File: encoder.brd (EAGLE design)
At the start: 25.1 x 31.7 mm, 7 parts, among them SW1 ROTARTY_ENCODER

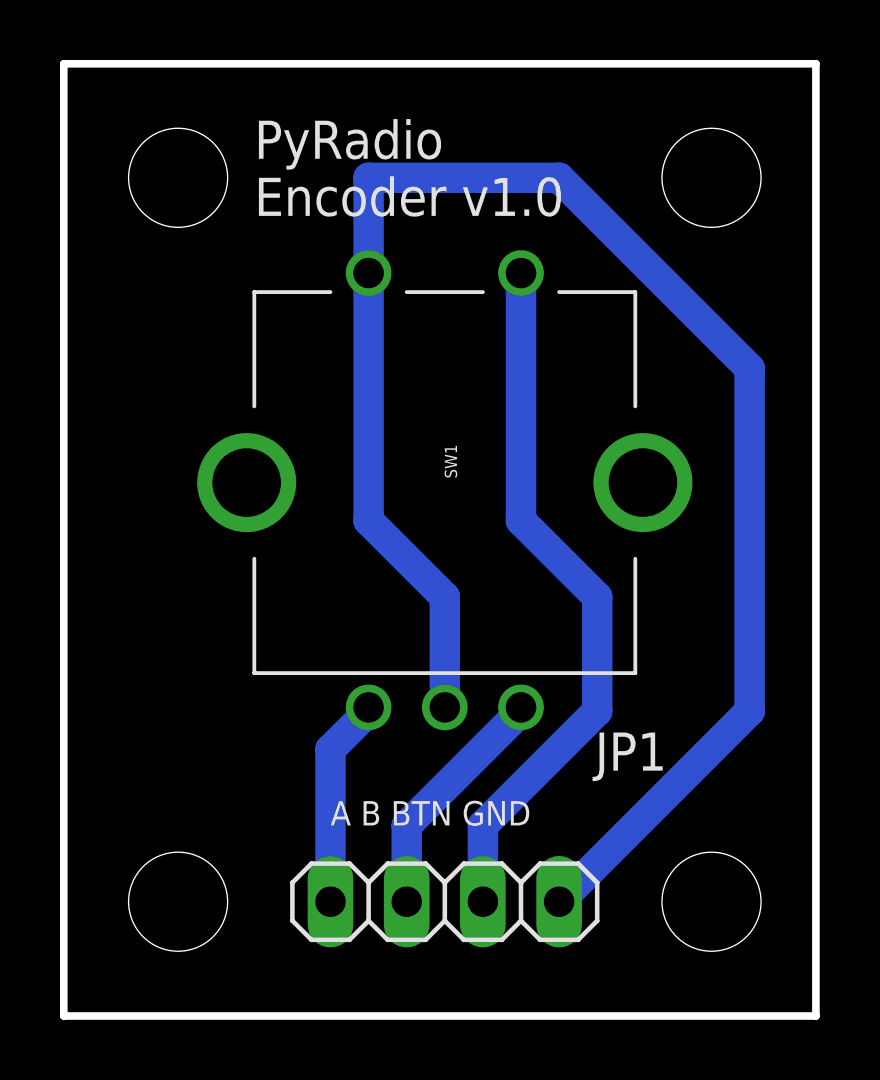
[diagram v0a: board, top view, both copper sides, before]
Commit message: pulled down all the eagle files on github.  histogram.py generates a histogram of the frequency of their usage.  You can make all the boards on github with ~1460 unique parts
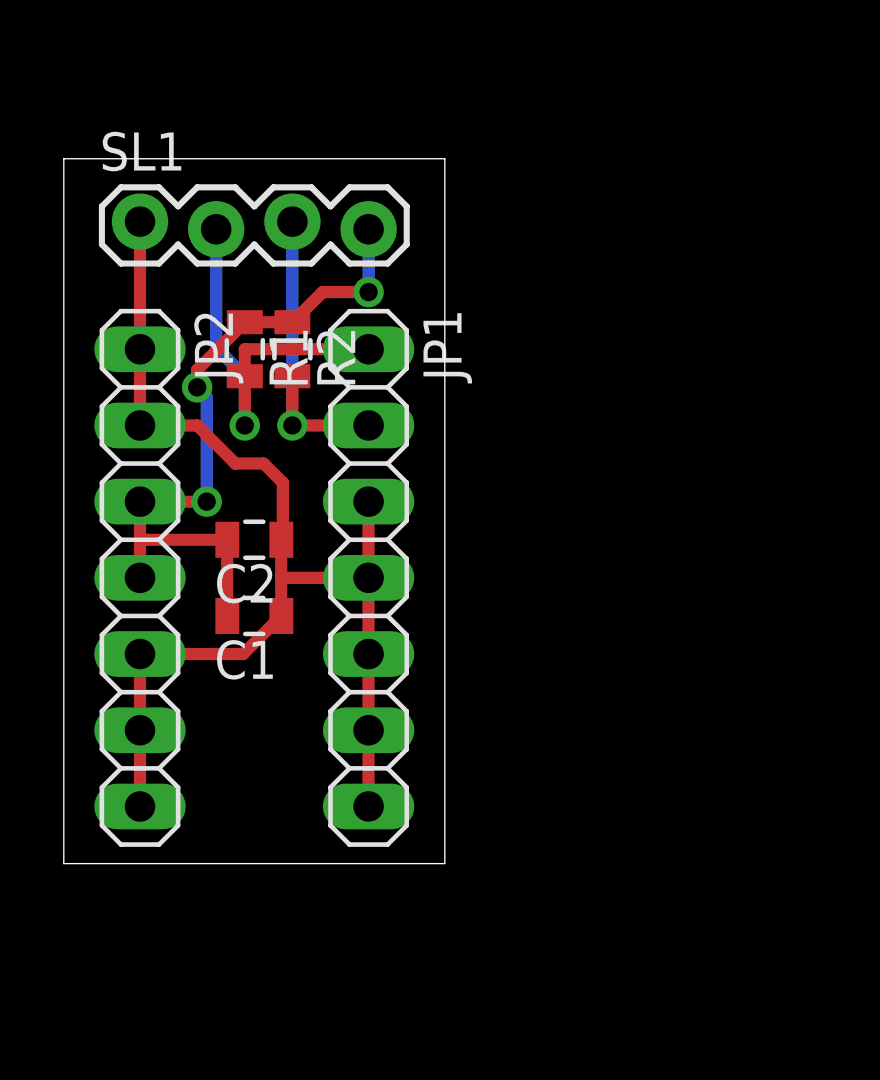
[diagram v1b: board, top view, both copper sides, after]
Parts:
- removed FRAME1: FRAME-LETTER, SparkFun-Aesthetics:CREATIVE_COMMONS
- removed STANDOFF1, STANDOFF2, STANDOFF3, STANDOFF4: STAND-OFF, SparkFun-Electromechanical:STAND-OFF
- removed SW1: ROTARTY_ENCODER, SparkFun-Electromechanical:ROTARY_ENC_PLAIN
- added C1: 47uF, ASL:0805
- added C2: .1uF, ASL:0805
- added JP2: (no value), baro:1X07
- added R1, R2: 4.7k, ASL:0805
- added SL1: (no value), ASL:1X04_LOCK
- JP1: device pinhead:1X04 -> baro:1X07
- moved JP1 11.1 mm to (10.2, 14.6), turned to 270 degrees
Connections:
- removed net A: JP1.1, SW1.A
- removed net B: JP1.2, SW1.B
- removed net BTN: JP1.3, SW1.SW+
- new net N$1: JP1.1, R1.2, SL1.2
- new net N$2: JP1.2, R2.2, SL1.3
- new net VCC: C1.2, C2.2, JP2.3, JP2.4, R1.1, R2.1, SL1.4
- net GND: now also C1.1, C2.1, JP1.3, JP1.5, JP1.6, JP1.7, JP2.1, JP2.2, JP2.5, JP2.6, JP2.7, SL1.1; no longer SW1.C, SW1.SW-
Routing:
- net VCC: track 0.00 -> 23.6 mm, vias 0 -> 3
- net BTN: track 23.6 -> 0.00 mm
- net GND: track 54.4 -> 40.2 mm
- net N$1: track 0.00 -> 13.6 mm, vias 0 -> 1
- net N$2: track 0.00 -> 11.0 mm, vias 0 -> 1
- net B: track 8.06 -> 0.00 mm
- net A: track 7.00 -> 0.00 mm
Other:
- board size 25.1 x 31.7 mm -> 12.7 x 23.5 mm
- board text removed: "A B BTN GND"
- board text removed: "PyRadio Encoder v1.0"
